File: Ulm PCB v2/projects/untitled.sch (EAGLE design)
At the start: 27 parts, among them U1 FT232RLSSOP, U2 MCP73831, U3 SPX3819-3.3, U4 RFM69HCW, X2 USB-SMD-NS

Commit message: Fixed Cap. Values for better voltage stabilazation
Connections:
- removed net +3V3: LED5.A
- removed net N$16: U4.GND@1
- removed net VCC: U4.VDD
- net 3.3V: now also C6.1, LED5.A, U4.VDD
- net GND: now also U4.GND@1
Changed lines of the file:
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@@
 <part name="U$1" library="arduinopromini" deviceset="ARDUINO_PRO_MINI" device=""/>
 <part name="GND4" library="supply1" deviceset="GND" device=""/>
-<part name="GND6" library="supply1" deviceset="GND" device=""/>
 <part name="C2" library="rcl" library_urn="urn:adsk.eagle:library:334" deviceset="C-EU" device="C0805" value="0.1uF"/>
 <part name="C5" library="SparkFun" deviceset="CAP_POL" device="1206" value="10uF"/>
@@
 <part name="J2" library="SparkFun-Connectors" deviceset="JST_2MM_MALE" device=""/>
 <part name="GND9" library="supply1" deviceset="GND" device=""/>
-<part name="P+3" library="supply1" deviceset="VCC" device=""/>
 <part name="C6" library="rcl" library_urn="urn:adsk.eagle:library:334" deviceset="C-EU" device="C0805" value="100n"/>
 <part name="C7" library="rcl" deviceset="C-EU" device="C0805" value="100n"/>
 <part name="GND15" library="supply1" deviceset="GND" device=""/>
-<part name="GND13" library="supply1" deviceset="GND" device=""/>
 <part name="GND16" library="supply1" deviceset="GND" device=""/>
 <part name="C8" library="rcl" library_urn="urn:adsk.eagle:library:334" deviceset="C-EU" device="C0805" value="10µF"/>
@@
 <part name="GND1" library="supply1" deviceset="GND" device=""/>
 <part name="GND10" library="supply1" deviceset="GND" device=""/>
-<part name="P+2" library="supply1" deviceset="VCC" device=""/>
-<part name="P+4" library="supply1" deviceset="VCC" device=""/>
 <part name="D3" library="microbuilder" deviceset="DIODE-SCHOTTKY" device="SOD-123" value="MBR120"/>
+<part name="+3V2" library="supply1" deviceset="+3V3" device="" value="3.3V"/>
 </parts>
 <sheets>
@@
 <instance part="U$1" gate="G$1" x="170.18" y="403.86"/>
 <instance part="GND4" gate="1" x="200.66" y="406.4"/>
-<instance part="GND6" gate="1" x="172.72" y="370.84"/>
 <instance part="C2" gate="G$1" x="-142.24" y="215.9"/>
 <instance part="C5" gate="G$1" x="-132.08" y="218.44"/>
@@
 <instance part="J2" gate="G$1" x="5.08" y="312.42" rot="R270"/>
 <instance part="GND9" gate="1" x="-2.54" y="284.48"/>
-<instance part="P+3" gate="VCC" x="104.14" y="434.34"/>
 <instance part="C6" gate="G$1" x="121.92" y="297.18"/>
 <instance part="C7" gate="G$1" x="200.66" y="414.02"/>
 <instance part="GND15" gate="1" x="121.92" y="289.56"/>
-<instance part="GND13" gate="1" x="93.98" y="383.54"/>
 <instance part="GND16" gate="1" x="157.48" y="281.94"/>
 <instance part="C8" gate="G$1" x="-154.94" y="403.86"/>
@@
 <instance part="U4" gate="G$1" x="83.82" y="299.72"/>
 <instance part="GND1" gate="1" x="50.8" y="279.4"/>
-<instance part="GND10" gate="1" x="111.76" y="279.4"/>
-<instance part="P+2" gate="VCC" x="104.14" y="434.34"/>
-<instance part="P+4" gate="VCC" x="121.92" y="320.04"/>
+<instance part="GND10" gate="1" x="111.76" y="274.32"/>
 <instance part="D3" gate="G$1" x="-160.02" y="429.26" rot="R270"/>
+<instance part="+3V2" gate="G$1" x="121.92" y="320.04" rot="MR0"/>
 </instances>
 <busses>
-<bus name="SCL,MISO,MOSI,CS,D4,D5,D6,D7">
-<segment>
-<wire x1="208.28" y1="391.16" x2="208.28" y2="358.14" width="0.762" layer="92"/>
-<wire x1="208.28" y1="358.14" x2="129.54" y2="358.14" width="0.762" layer="92"/>
-</segment>
-</bus>
 </busses>
 <nets>
@@
 <pinref part="GND1" gate="1" pin="GND"/>
 </segment>
+<segment>
+<pinref part="U4" gate="G$1" pin="GND@1"/>
+<wire x1="96.52" y1="292.1" x2="111.76" y2="292.1" width="0.1524" layer="91"/>
+<wire x1="111.76" y1="292.1" x2="111.76" y2="276.86" width="0.1524" layer="91"/>
+<pinref part="GND10" gate="1" pin="GND"/>
+</segment>
 </net>
 <net name="USB_D-" class="0">
@@
 <wire x1="200.66" y1="416.56" x2="185.42" y2="416.56" width="0.1524" layer="91"/>
 <junction x="200.66" y="416.56"/>
-</segment>
-<segment>
-<pinref part="P+3" gate="VCC" pin="VCC"/>
-<pinref part="P+2" gate="VCC" pin="VCC"/>
 </segment>
 <segment>
@@
 <pinref part="3.3V" gate="G$1" pin="5V"/>
 </segment>
+<segment>
+<pinref part="LED5" gate="G$1" pin="A"/>
+<wire x1="-134.62" y1="299.72" x2="-139.7" y2="299.72" width="0.1524" layer="91"/>
+<wire x1="-139.7" y1="299.72" x2="-139.7" y2="322.58" width="0.1524" layer="91"/>
+<pinref part="+3V1" gate="G$1" pin="+3V3"/>
+</segment>
+<segment>
+<pinref part="U4" gate="G$1" pin="VDD"/>
+<wire x1="96.52" y1="299.72" x2="121.92" y2="299.72" width="0.1524" layer="91"/>
+<wire x1="121.92" y1="299.72" x2="121.92" y2="317.5" width="0.1524" layer="91"/>
+<pinref part="C6" gate="G$1" pin="1"/>
+<junction x="121.92" y="299.72"/>
+<pinref part="+3V2" gate="G$1" pin="+3V3"/>
+</segment>
 </net>
 <net name="TXLED" class="0">
@@
 </segment>
 </net>
-<net name="+3V3" class="0">
-<segment>
-<pinref part="LED5" gate="G$1" pin="A"/>
-<wire x1="-134.62" y1="299.72" x2="-139.7" y2="299.72" width="0.1524" layer="91"/>
-<wire x1="-139.7" y1="299.72" x2="-139.7" y2="322.58" width="0.1524" layer="91"/>
-<pinref part="+3V1" gate="G$1" pin="+3V3"/>
-</segment>
-</net>
-<net name="N$16" class="0">
-<segment>
-<pinref part="U4" gate="G$1" pin="GND@1"/>
-<wire x1="96.52" y1="292.1" x2="111.76" y2="292.1" width="0.1524" layer="91"/>
-<wire x1="111.76" y1="292.1" x2="111.76" y2="281.94" width="0.1524" layer="91"/>
-</segment>
-</net>
-<net name="VCC" class="0">
-<segment>
-<pinref part="U4" gate="G$1" pin="VDD"/>
-<wire x1="96.52" y1="299.72" x2="121.92" y2="299.72" width="0.1524" layer="91"/>
-<wire x1="121.92" y1="299.72" x2="121.92" y2="317.5" width="0.1524" layer="91"/>
-<pinref part="P+4" gate="VCC" pin="VCC"/>
-</segment>
-</net>

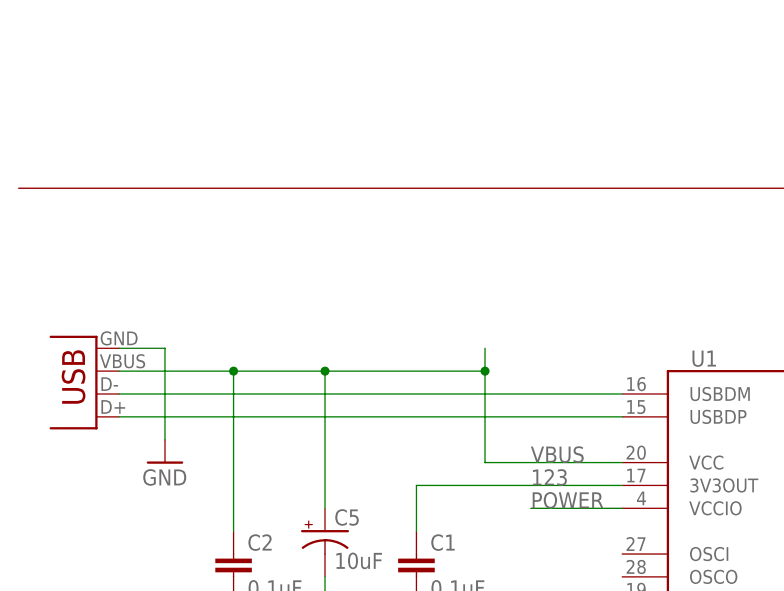
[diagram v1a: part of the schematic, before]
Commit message: added microUSB
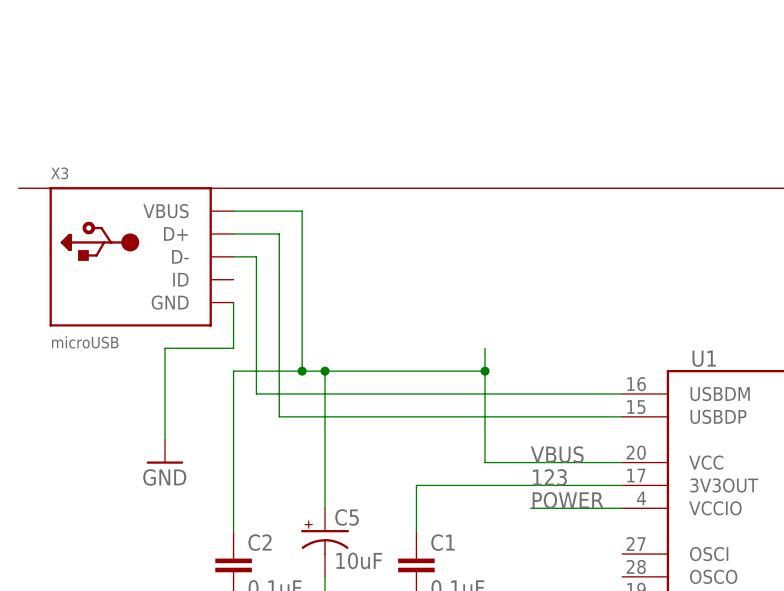
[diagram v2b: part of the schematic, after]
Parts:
- removed X2: USB-SMD-NS, SparkFun:USB-SMD-NS
- added X3: microUSB, microbuilder:USB_MICRO_20329_V2
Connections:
- net GND: now also X3.GND; no longer X2.GND
- net USB_D+: now also X3.D+; no longer X2.D+
- net USB_D-: now also X3.D-; no longer X2.D-
- net VBUS: now also X3.VBUS; no longer X2.VBUS
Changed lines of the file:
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@@
 <part name="C5" library="SparkFun" deviceset="CAP_POL" device="1206" value="10uF"/>
 <part name="C1" library="rcl" library_urn="urn:adsk.eagle:library:334" deviceset="C-EU" device="C0805" value="0.1uF"/>
-<part name="X2" library="SparkFun" deviceset="USB" device="-SMD-NS"/>
 <part name="GND2" library="SparkFun" deviceset="GND" device=""/>
 <part name="GND3" library="SparkFun" deviceset="GND" device=""/>
@@
 <part name="D3" library="microbuilder" deviceset="DIODE-SCHOTTKY" device="SOD-123" value="MBR120"/>
 <part name="+3V2" library="supply1" deviceset="+3V3" device="" value="3.3V"/>
+<part name="X3" library="microbuilder" deviceset="USB" device="_MICRO_20329_V2" value="microUSB"/>
 </parts>
 <sheets>
@@
 <instance part="C5" gate="G$1" x="-132.08" y="218.44"/>
 <instance part="C1" gate="G$1" x="-121.92" y="215.9"/>
-<instance part="X2" gate="G$1" x="-157.48" y="238.76" rot="R180"/>
 <instance part="GND2" gate="1" x="-121.92" y="208.28"/>
 <instance part="GND3" gate="1" x="-101.6" y="193.04"/>
@@
 <instance part="D3" gate="G$1" x="-160.02" y="429.26" rot="R270"/>
 <instance part="+3V2" gate="G$1" x="121.92" y="320.04" rot="MR0"/>
+<instance part="X3" gate="G$1" x="-152.4" y="248.92"/>
 </instances>
 <busses>
@@
 </segment>
 <segment>
-<wire x1="-154.94" y1="238.76" x2="-149.86" y2="238.76" width="0.1524" layer="91"/>
 <wire x1="-149.86" y1="238.76" x2="-149.86" y2="228.6" width="0.1524" layer="91"/>
-<pinref part="X2" gate="G$1" pin="GND"/>
 <pinref part="GND5" gate="1" pin="GND"/>
+<pinref part="X3" gate="G$1" pin="GND"/>
+<wire x1="-142.24" y1="243.84" x2="-142.24" y2="238.76" width="0.1524" layer="91"/>
+<wire x1="-142.24" y1="238.76" x2="-149.86" y2="238.76" width="0.1524" layer="91"/>
 </segment>
 <segment>
@@
 <net name="USB_D-" class="0">
 <segment>
-<wire x1="-99.06" y1="233.68" x2="-154.94" y2="233.68" width="0.1524" layer="91"/>
-<pinref part="X2" gate="G$1" pin="D-"/>
+<wire x1="-99.06" y1="233.68" x2="-139.7" y2="233.68" width="0.1524" layer="91"/>
 <pinref part="U1" gate="G$1" pin="USBDM"/>
+<pinref part="X3" gate="G$1" pin="D-"/>
+<wire x1="-142.24" y1="248.92" x2="-139.7" y2="248.92" width="0.1524" layer="91"/>
+<wire x1="-139.7" y1="248.92" x2="-139.7" y2="233.68" width="0.1524" layer="91"/>
 </segment>
 </net>
 <net name="USB_D+" class="0">
 <segment>
-<wire x1="-99.06" y1="231.14" x2="-154.94" y2="231.14" width="0.1524" layer="91"/>
-<pinref part="X2" gate="G$1" pin="D+"/>
+<wire x1="-99.06" y1="231.14" x2="-137.16" y2="231.14" width="0.1524" layer="91"/>
 <pinref part="U1" gate="G$1" pin="USBDP"/>
+<pinref part="X3" gate="G$1" pin="D+"/>
+<wire x1="-142.24" y1="251.46" x2="-137.16" y2="251.46" width="0.1524" layer="91"/>
+<wire x1="-137.16" y1="251.46" x2="-137.16" y2="231.14" width="0.1524" layer="91"/>
 </segment>
 </net>
@@
 <net name="VBUS" class="0">
 <segment>
-<wire x1="-142.24" y1="236.22" x2="-132.08" y2="236.22" width="0.1524" layer="91"/>
+<wire x1="-142.24" y1="236.22" x2="-134.62" y2="236.22" width="0.1524" layer="91"/>
+<wire x1="-134.62" y1="236.22" x2="-132.08" y2="236.22" width="0.1524" layer="91"/>
 <wire x1="-132.08" y1="236.22" x2="-114.3" y2="236.22" width="0.1524" layer="91"/>
 <wire x1="-114.3" y1="236.22" x2="-114.3" y2="226.06" width="0.1524" layer="91"/>
@@
 <wire x1="-132.08" y1="220.98" x2="-132.08" y2="236.22" width="0.1524" layer="91"/>
 <wire x1="-142.24" y1="218.44" x2="-142.24" y2="236.22" width="0.1524" layer="91"/>
-<wire x1="-154.94" y1="236.22" x2="-142.24" y2="236.22" width="0.1524" layer="91"/>
 <wire x1="-114.3" y1="238.76" x2="-114.3" y2="236.22" width="0.1524" layer="91"/>
 <junction x="-132.08" y="236.22"/>
-<junction x="-142.24" y="236.22"/>
 <junction x="-114.3" y="236.22"/>
 <label x="-109.22" y="226.06" size="1.778" layer="95"/>
@@
 <pinref part="C5" gate="G$1" pin="+"/>
 <pinref part="C2" gate="G$1" pin="1"/>
-<pinref part="X2" gate="G$1" pin="VBUS"/>
-</segment>
-<segment>
+<pinref part="X3" gate="G$1" pin="VBUS"/>
+<wire x1="-142.24" y1="254" x2="-134.62" y2="254" width="0.1524" layer="91"/>
+<wire x1="-134.62" y1="254" x2="-134.62" y2="236.22" width="0.1524" layer="91"/>
+<junction x="-134.62" y="236.22"/>
+</segment>
+<segment>
